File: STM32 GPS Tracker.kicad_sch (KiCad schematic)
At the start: 24 parts, among them J3 693010020611, Q1 AO3407A, U1 SIM808, U2 TPS5430DDA, U3 SMF05CT1G, U4 STM32F030C8Tx

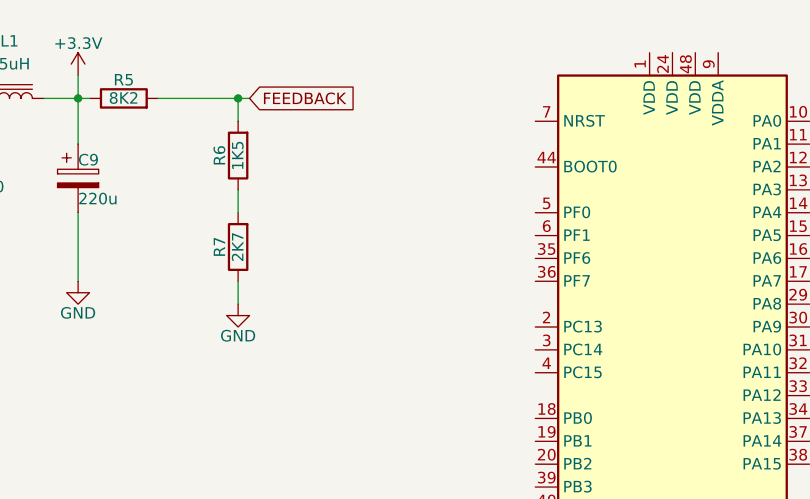
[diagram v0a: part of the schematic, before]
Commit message: Completed Placing and wiring components for Voltage regulation ckt in Schematic
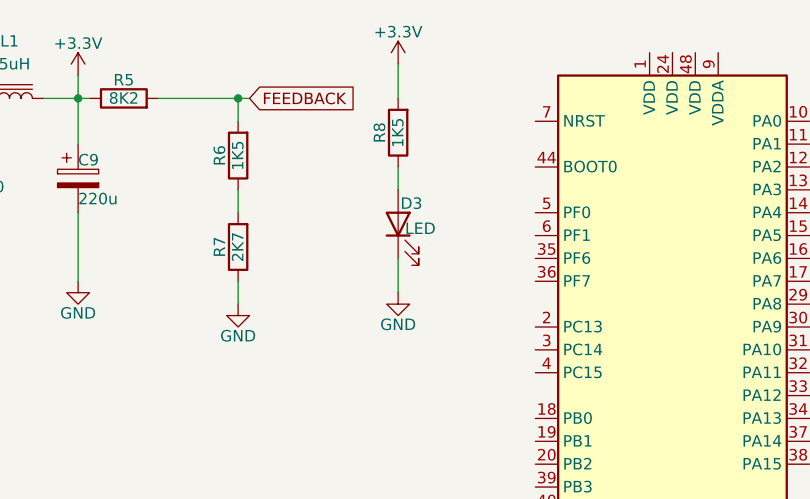
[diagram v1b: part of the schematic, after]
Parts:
- added D3: LED, symbol Device:LED
- added R8: 1K5, symbol Device:R
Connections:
- net +3.3V: now also R8.2
- net GND: now also D3.1 (K)
- new net: D3.2 (A), R8.1

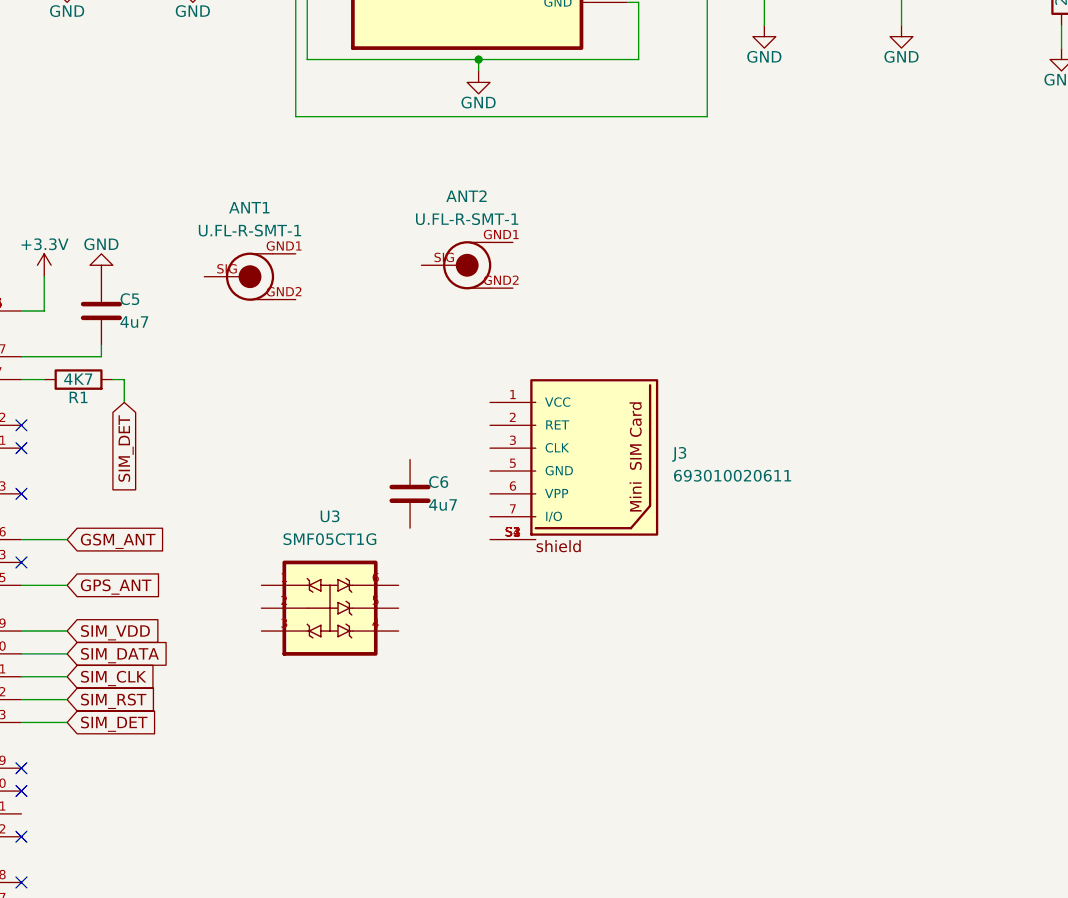
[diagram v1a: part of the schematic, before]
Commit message: Completed Placing and Wiring components for SIM SOCKET in Schematic
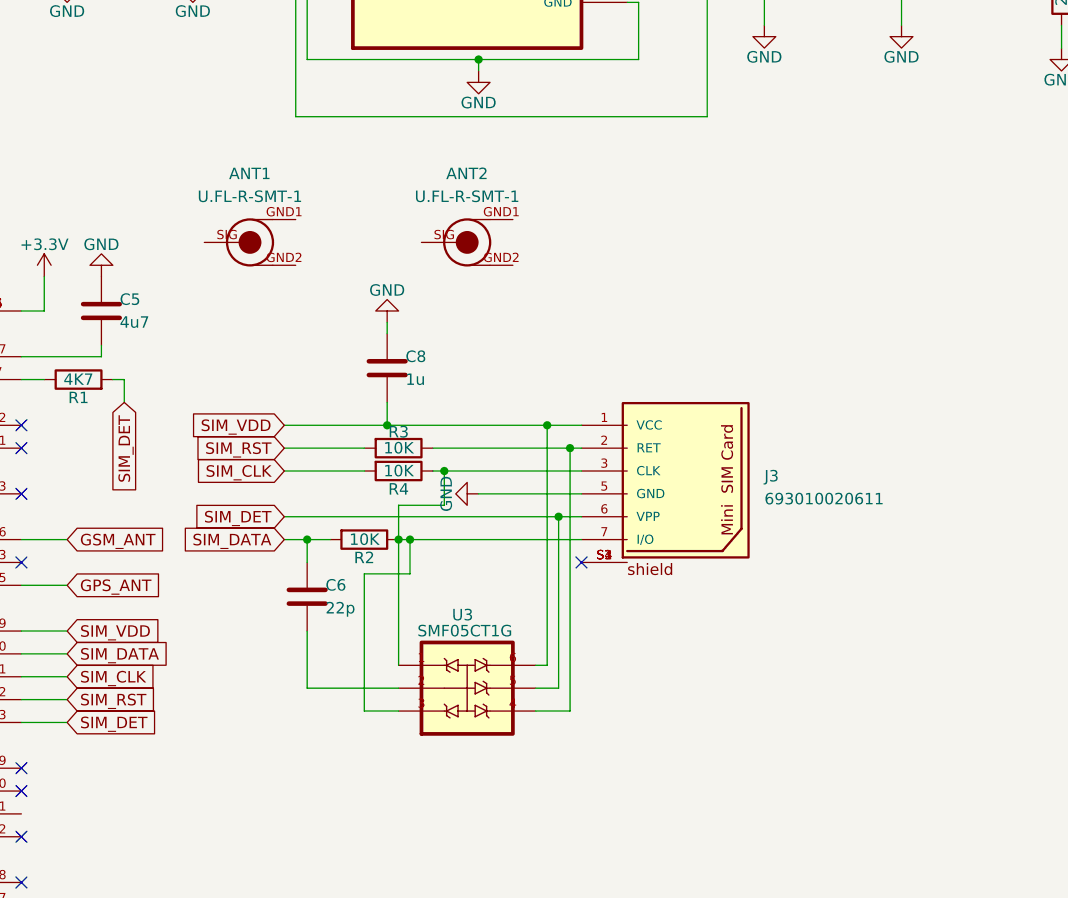
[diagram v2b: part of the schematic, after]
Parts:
- added C8: 1u, symbol Device:C
- added R2, R3, R4: 10K, symbol Device:R
- C6: value 4u7 -> 22p
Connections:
- net GND: now also J3.5 (GND), C8.1
- net SIM_CLK: now also R4.2
- net SIM_DATA: now also C6.1, R2.2
- net SIM_DET: now also J3.6 (VPP), U3.5
- net SIM_RST: now also R3.2
- net SIM_VDD: now also J3.1 (VCC), U3.6, C8.2
- net at C6.2: now also U3.2
- net at J3.2 (RET): now also U3.4, R3.1
- net at J3.3 (CLK): now also J3.7 (I/O), U3.1, U3.3, R2.1, R4.1
- no-connect marks 36 -> 37
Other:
- moved on the sheet: ANT1, ANT2, C6, J3, U3

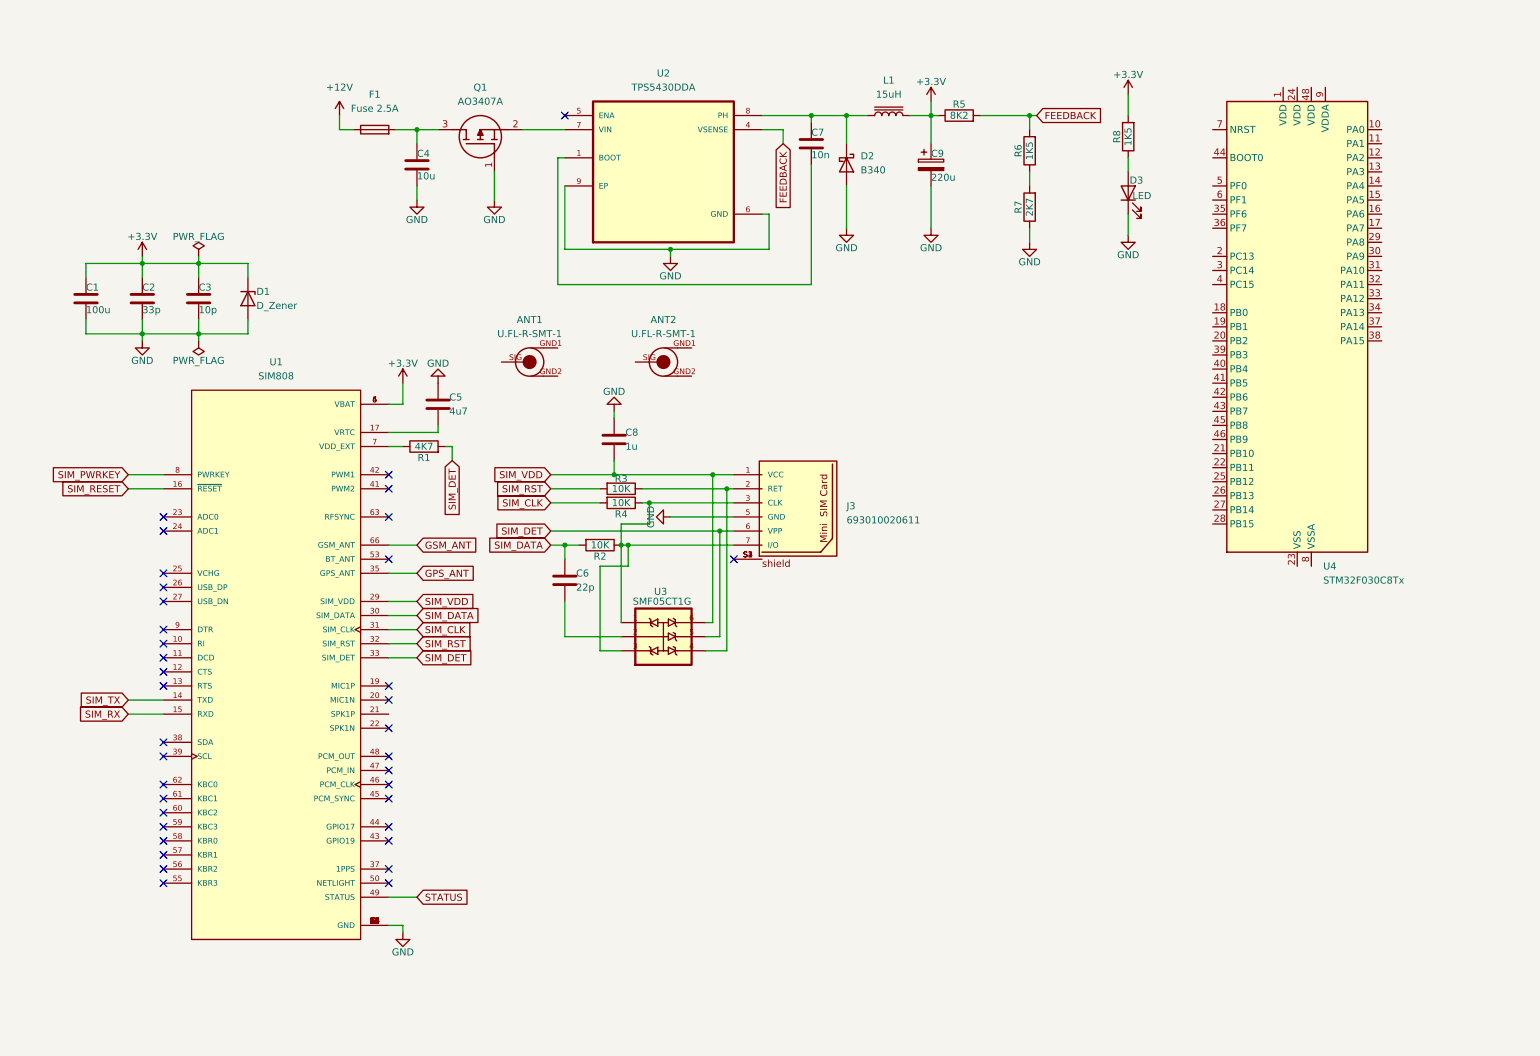
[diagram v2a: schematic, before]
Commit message: Placing and wiring components for STM32 ckt in Schematic
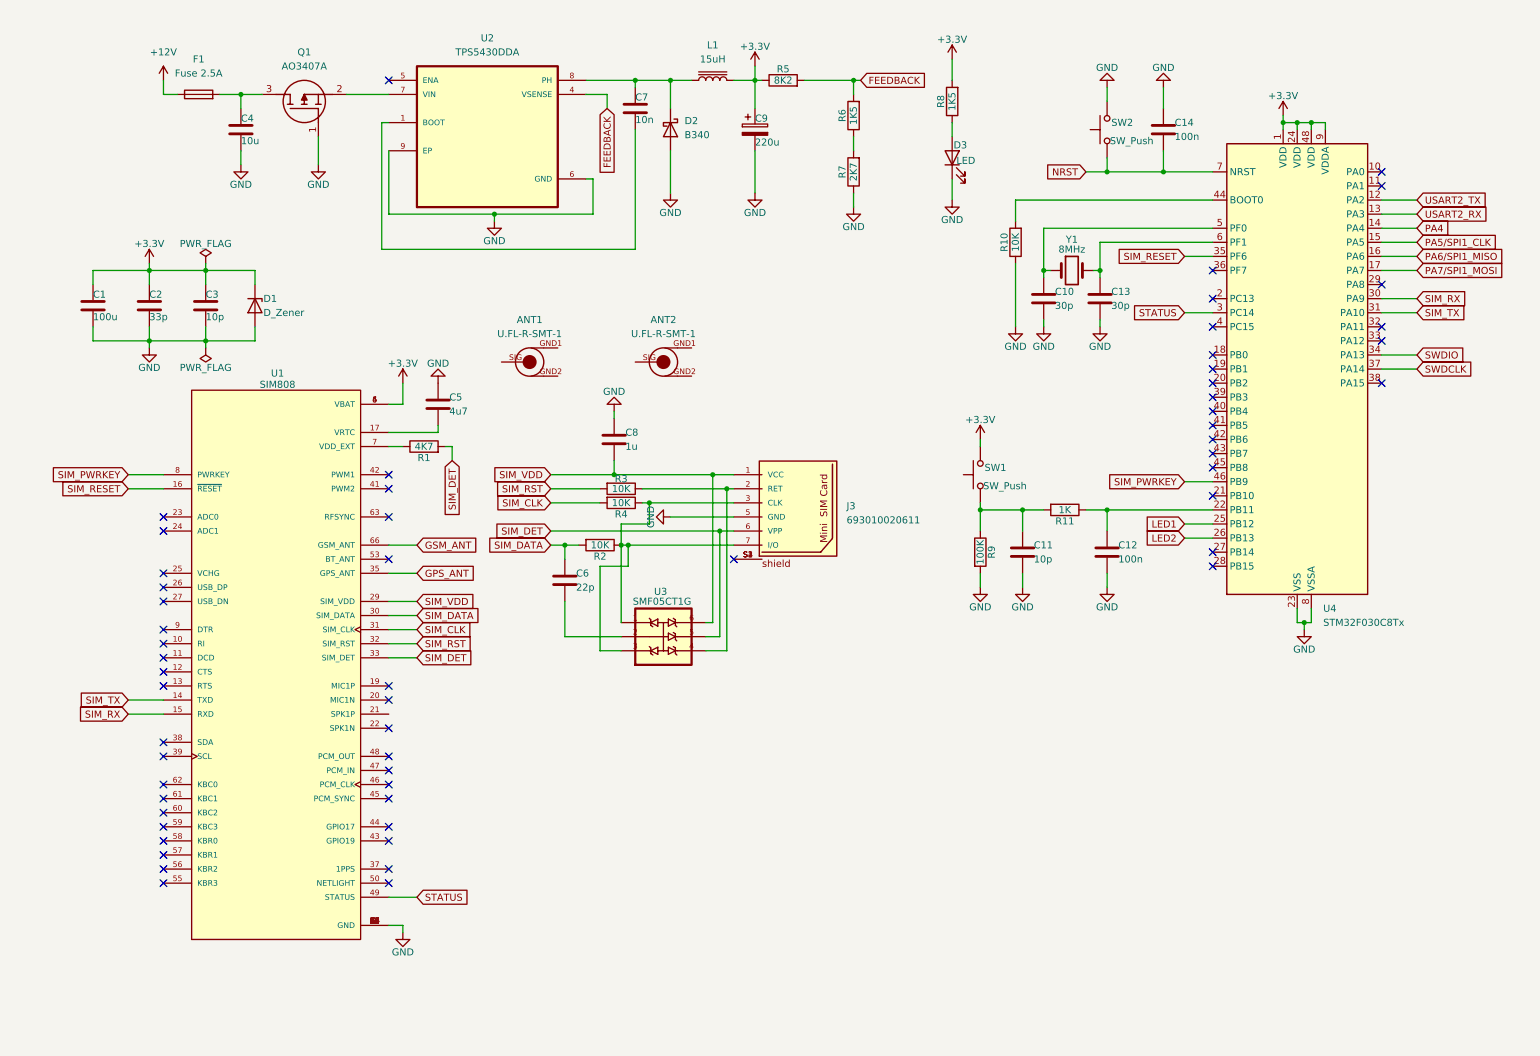
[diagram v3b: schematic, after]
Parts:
- added C10, C13: 30p, symbol Device:C
- added C11: 10p, symbol Device:C
- added C12, C14: 100n, symbol Device:C
- added R10: 10K, symbol Device:R
- added R11: 1K, symbol Device:R
- added R9: 100K, symbol Device:R
- added SW1, SW2: SW_Push, symbol Switch:SW_Push
- added Y1: 8MHz, symbol Device:Crystal
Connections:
- net +3.3V: now also U4.1 (VDD), U4.24 (VDD), U4.48 (VDD), U4.9 (VDDA), SW1.2
- net GND: now also U4.23 (VSS), U4.47 (VSS), U4.8 (VSSA), C10.2, C11.2, C12.2, C13.2, C14.1, R10.1, R9.2, SW2.2
- net SIM_PWRKEY: now also U4.46 (PB9)
- net SIM_RESET: now also U4.35 (PF6)
- net SIM_RX: now also U4.30 (PA9)
- net SIM_TX: now also U4.31 (PA10)
- net STATUS: now also U4.3 (PC14)
- net USART2_TX: now reaches U4.12 (PA2)
- net USART2_RX: now reaches U4.13 (PA3)
- net PA4: now reaches U4.14 (PA4)
- net PA5/SPI1_CLK: now reaches U4.15 (PA5)
- net PA6/SPI1_MISO: now reaches U4.16 (PA6)
- net PA7/SPI1_MOSI: now reaches U4.17 (PA7)
- net at U4.22 (PB11): now also C12.1, R11.1
- net LED1: now reaches U4.25 (PB12)
- net LED2: now reaches U4.26 (PB13)
- net SWDIO: now reaches U4.34 (PA13)
- net SWDCLK: now reaches U4.37 (PA14)
- net at U4.44 (BOOT0): now also R10.2
- net at U4.5 (PF0): now also C10.1, Y1.1
- net at U4.6 (PF1): now also C13.1, Y1.2
- net NRST: now reaches U4.7 (NRST)
- net NRST: now also C14.2, SW2.1
- new net: C11.1, R11.2, R9.1, SW1.1
- no-connect marks 37 -> 58
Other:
- moved on the sheet: C1, C2, C3, C4, C7, C9, D1, D2, D3, F1, L1, Q1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

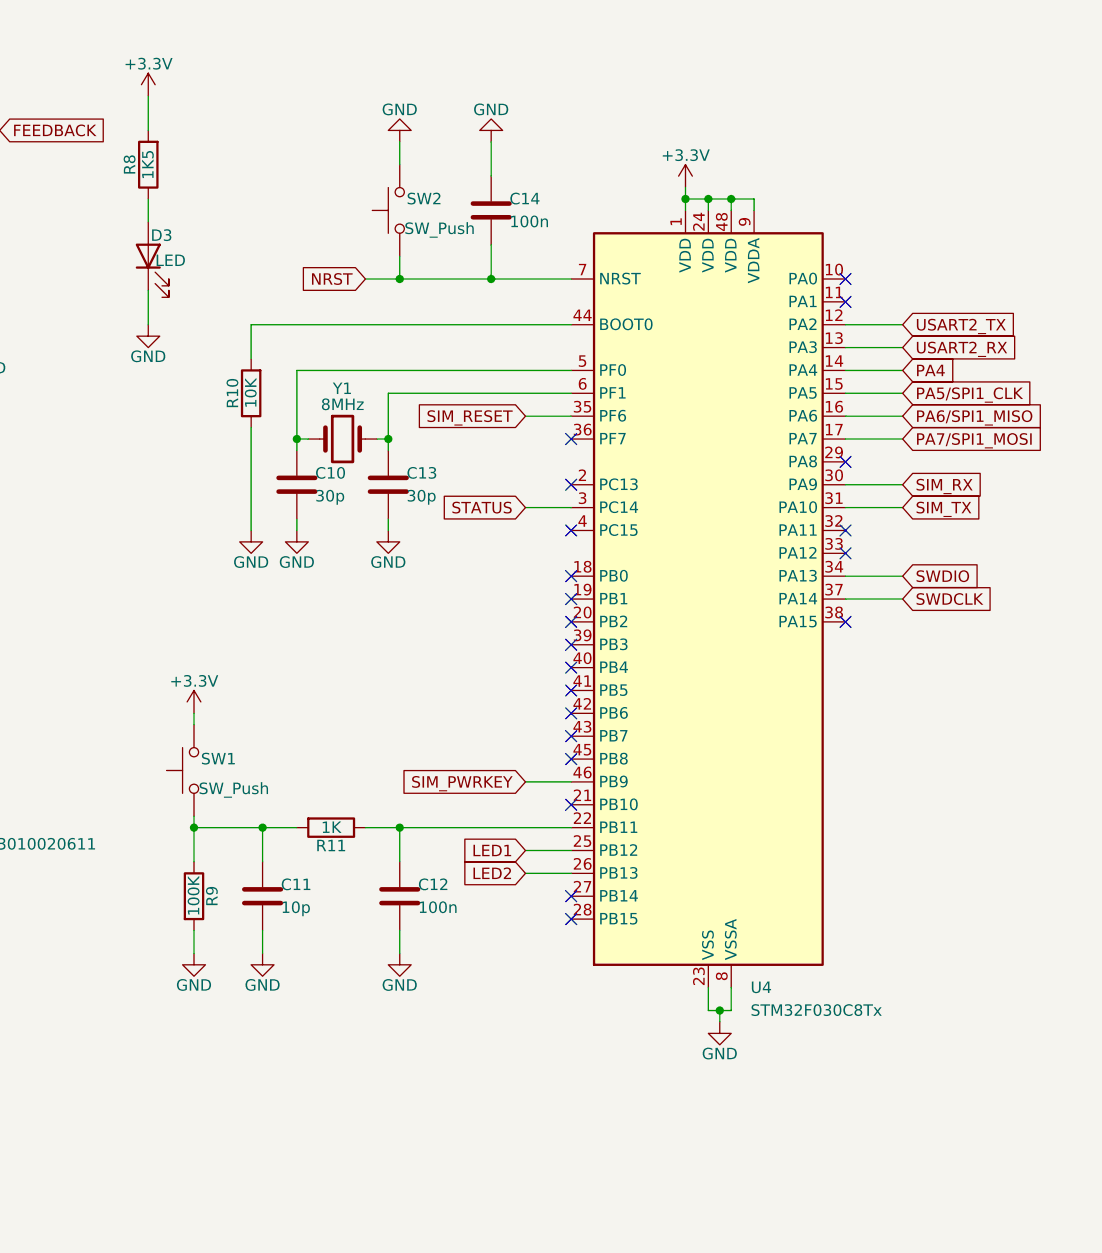
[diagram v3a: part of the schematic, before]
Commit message: Remaining Placing and wiring components for STM32 ckt in Schematic
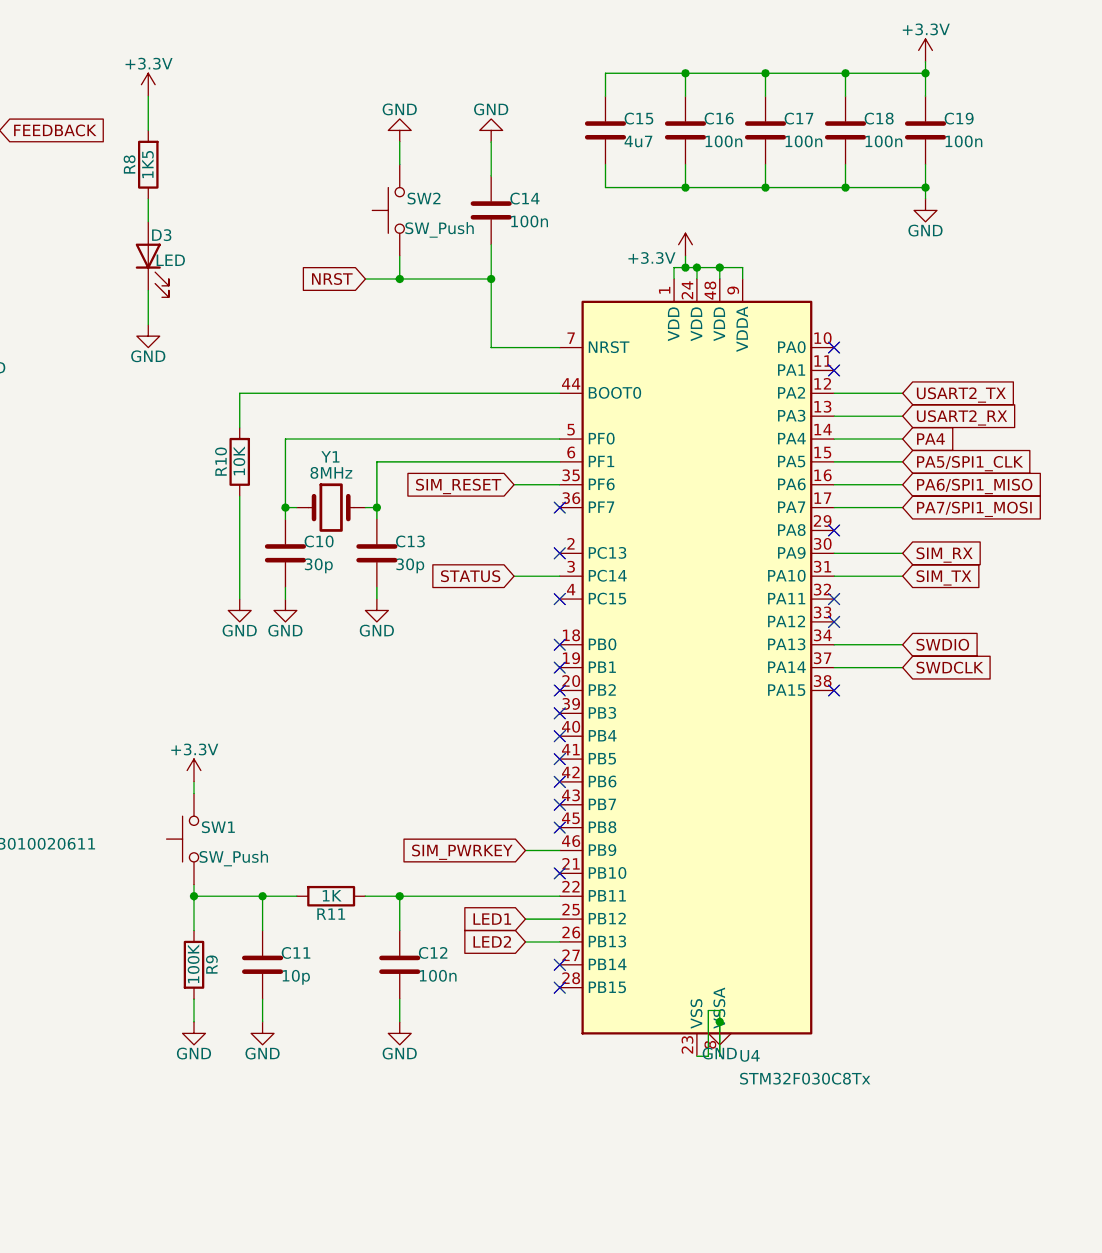
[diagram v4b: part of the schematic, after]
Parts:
- added C15: 4u7, symbol Device:C
- added C16, C17, C18, C19: 100n, symbol Device:C
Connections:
- net +3.3V: now also C15.1, C16.1, C17.1, C18.1, C19.1
- net GND: now also C15.2, C16.2, C17.2, C18.2, C19.2
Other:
- moved on the sheet: C10, C11, C12, C13, R10, R11, R9, SW1, U4, Y1
